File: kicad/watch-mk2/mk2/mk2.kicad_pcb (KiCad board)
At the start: 2 copper layers, 30 x 60 mm, 71 parts, among them IC1 113990582, IC2 M41T62LC6F, J1 FPC24-0.5mm, J2 USB_C_Receptacle_USB2.0, J3 Conn_01x02_Female, Q1 Si1308EDL, Q2 Si1308EDL, Q3 Si1308EDL, Q4 Si1308EDL, SW1 B5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

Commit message: add rev2mk2
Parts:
- removed C11, C12, C13, C14, C15, C16, C17, C18, C19: 1uF, Capacitor_SMD:C_0603_1608Metric_Pad1.05x0.95mm_HandSolder
- removed D3, D4, D5: MBR0530, Diode_SMD:D_SOD-123
- removed D6: CHRG_LED, LED_SMD:LED_0603_1608Metric_Pad1.05x0.95mm_HandSolder
- removed D7: FLASHLIGHT, Connector_PinHeader_2.54mm:PinHeader_1x02_P2.54mm_Vertical
- removed D8: BACKLIGHT, Connector_PinHeader_2.54mm:PinHeader_1x02_P2.54mm_Vertical
- removed Q1, Q2: Si1308EDL, Package_TO_SOT_SMD:SOT-323_SC-70
- removed R1, R2: 1k, Resistor_SMD:R_0603_1608Metric_Pad1.05x0.95mm_HandSolder
- removed R10: 470, Resistor_SMD:R_0603_1608Metric_Pad1.05x0.95mm_HandSolder
- removed R7: 10k, Resistor_SMD:R_0603_1608Metric_Pad1.05x0.95mm_HandSolder
- removed R8: 3, Resistor_SMD:R_0603_1608Metric_Pad1.05x0.95mm_HandSolder
- removed SW3: B2, libs:E-Switch-TL3330AF130QG-MFG
- removed SW5: B4, libs:E-Switch-TL3330AF130QG-MFG
- removed SW_BOOT1: SW_Push, Button_Switch_SMD:SW_SPST_CK_KXT3
- added J5: Conn_01x04_Female, libs:ffc-0.5mm-4, F.Cu at (31.2, 35.2)
- added JP1: FUEL_BYP, Resistor_SMD:R_0603_1608Metric, F.Cu at (34.6, 42.6)
- added P1: AXT610124, libs:PANASONIC_AXT610124, F.Cu at (31.5, 38.0)
- added U5: MAX17220ELT+, max17220:Maxim_Integrated-L622-1C-0-E-IPC_A, F.Cu at (18.0, 14.5)
- added U6: MAX17262REWL+T, max17262:Maxim-W91G1-3-0-A-IPC_A, F.Cu at (28.0, 45.0)
- BT1: footprint Connector_JST:JST_PH_B2B-PH-K_1x02_P2.00mm_Vertical -> Connector_JST:JST_SH_BM02B-SRSS-TB_1x02-1MP_P1.00mm_Vertical; moved to F.Cu
- C10: value 1uF -> 0.47uF; moved to F.Cu
- C20, D1, J2, R6, SW_RESET1: moved to F.Cu
- C6: value 4.7uF -> 10uF; moved to F.Cu
- C8: value 4.7uF -> 10uF
- C9: value 1uF -> 560pF; moved to F.Cu
- IC1: value 113990582 -> MDBT50Q
- J1: value FPC24-0.5mm -> Conn_01x10_Female; footprint Connector_FFC-FPC:Hirose_FH12-24S-0.5SH_1x24-1MP_P0.50mm_Horizontal -> Connector_FFC-FPC:Hirose_FH12-10S-0.5SH_1x10-1MP_P0.50mm_Horizontal
- L2: value 10uH -> 2.2uH
- R13, R15: value 1k -> 100k
- R5: value 10k -> 100k
- U1: footprint Package_SO:TSSOP-8_4.4x3mm_P0.65mm -> libs:SON50P300X200X60-9N
- moved C9 51.6 mm to (23.0, 15.4), turned to 90 degrees
- moved J1 48.0 mm to (29.5, 17.5), turned to 180 degrees
- moved J3 40.7 mm to (18.0, 17.5), turned to -90 degrees
- moved C8 39.3 mm to (23.0, 18.9), turned to 90 degrees
- moved L2 37.6 mm to (20.5, 14.6), turned to 90 degrees
- moved R15 35.1 mm to (14.4, 23.2), turned to 180 degrees
- moved C6 35.1 mm to (20.4, 17.5), turned to 180 degrees
- moved SW2 33.6 mm to (14.0, 16.8), turned to -90 degrees
- moved BT1 32.8 mm to (32.5, 47.0)
- moved Q4 31.2 mm to (14.2, 25.5), turned to 180 degrees
- moved J2 30.7 mm to (21.5, 44.8)
- moved R16 29.7 mm to (14.4, 21.8), turned to 180 degrees
- moved TP3 27.3 mm to (30.5, 24.8), turned to 180 degrees
- moved SW1 26.7 mm to (14.0, 31.2), turned to -90 degrees
- moved TP4 26.6 mm to (28.2, 27.0), turned to 180 degrees
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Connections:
- C10 pad 1: GND -> Net-(C10-Pad1)
- C10 pad 2: /EPVPP -> GND
- C20 pad 1: +BATT -> BATTPOW
- C6 pad 1: GND -> VIN
- C6 pad 2: VCC -> GND
- C8 pad 1: Net-(C8-Pad1) -> 5V
- C8 pad 2: Net-(C8-Pad2) -> GND
- C9 pad 1: /EPPREVGH -> LCD_DISP
- D1 pad 1: +BATT -> VUSB
- D1 pad 2: VUSB -> BATTPOW
- IC1 pad 10: BUTTON1 -> SPI_CLK
- IC1 pad 12: BUTTON5 -> SPI_MOSI
- IC1 pad 13: SQW -> BUZZER
- IC1 pad 14: RTCIRQ -> SPI_MISO
- IC1 pad 16: SCL -> FLASH_CS
- IC1 pad 19: SDA -> (no net)
- IC1 pad 20: FLASH_CS -> (no net)
- IC1 pad 22: FLASH_DO -> BUTTON1
- IC1 pad 24: FLASH_CLK -> BUTTON5
- IC1 pad 26: FLASH_DI -> BUTTON3
- IC1 pad 3: BOOTLOAD -> LCD_CS
- IC1 pad 36: FLASHLIGHT -> (no net)
- IC1 pad 41: (no net) -> RTCIRQ
- IC1 pad 42: (no net) -> SQW
- IC1 pad 43: EPSDIN -> (no net)
- IC1 pad 44: EPSCLK -> SDA
- IC1 pad 45: EPCS -> (no net)
- IC1 pad 46: EPDC -> SCL
- IC1 pad 47: EPRES -> (no net)
- IC1 pad 48: EPBUSY -> BUTTON4
- IC1 pad 49: (no net) -> FLASHLIGHT
- IC1 pad 50: (no net) -> BUTTON2
- IC1 pad 52: BUTTON3 -> CHGNG
- IC1 pad 54: BUTTON4 -> (no net)
- IC1 pad 6: BUZZER -> (no net)
- IC1 pad 8: BUTTON2 -> (no net)
- J1 pad 1: (no net) -> SPI_CLK
- J1 pad 10: EPRES -> GND
- J1 pad 2: /EPGDR -> SPI_MOSI
- J1 pad 3: /EPRESE -> LCD_CS
- J1 pad 4: /EPVGL -> SQW
- J1 pad 5: /EPVGH -> LCD_DISP
- J1 pad 6: (no net) -> 5V
- J1 pad 7: (no net) -> 5V
- J1 pad 8: GND -> 5V
- J1 pad 9: EPBUSY -> GND
- L2 pad 1: VCC -> VIN
- L2 pad 2: Net-(C8-Pad1) -> Net-(L2-Pad2)
- R5 pad 1: VCC -> CHGNG
- R5 pad 2: BOOTLOAD -> VCC
- TP1 pad 1: SWDIO -> GND
- TP4 pad 1: GND -> SWDIO
- U1 pad 2: FLASH_DO -> SPI_MISO
- U1 pad 5: FLASH_DI -> SPI_MOSI
- U1 pad 6: FLASH_CLK -> SPI_CLK
- U3 pad 1: Net-(R10-Pad1) -> CHGNG
- U3 pad 3: +BATT -> BATTPOW
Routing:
- net GND: track 66.2 -> 30.5 mm, vias 27 -> 33
- net EPSCLK: track 33.3 -> 0.00 mm, vias 2 -> 0
- net EPSDIN: track 31.5 -> 0.00 mm, vias 2 -> 0
- net EPCS: track 30.3 -> 0.00 mm, vias 2 -> 0
- net Net-(C8-Pad1): track 25.9 -> 0.00 mm, vias 2 -> 0
- net VCC: track 71.1 -> 46.0 mm, vias 14 -> 7
- net BATTPOW: track 0.00 -> 24.7 mm, vias 0 -> 4
- net VIN: track 25.5 -> 49.7 mm, vias 2 -> 6
- net EPRES: track 23.7 -> 0.00 mm, vias 2 -> 0
- net /EPPREVGH: track 23.6 -> 0.00 mm, vias 1 -> 0
- net EPDC: track 23.1 -> 0.00 mm, vias 2 -> 0
- net EPBUSY: track 22.7 -> 0.00 mm, vias 2 -> 0
- net SDA: track 9.68 -> 30.3 mm, vias 0 -> 3
- net SCL: track 7.17 -> 27.5 mm, vias 0 -> 3
- net CHGNG: track 0.00 -> 18.3 mm, vias 0 -> 4
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- added copper zone on In2.Cu, net GND
- added copper zone on In1.Cu, net VCC
- removed copper zone on B.Cu, net GND
- removed copper zone on F.Cu, net VCC
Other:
- board size 30 x 60 mm -> 23.5 x 37.5 mm
- copper layers 2 -> 4
- board text added: "+2.8v"
- board text added: "nrf52-watch mk2 - rev.2"
- board text removed: "+"
- board text removed: "+ -"
- board text removed: "+2.8V"
- board text removed: "-"
- board text removed: "Backlight"
- board text removed: "Flashlight"
- board text removed: "buzzer"
- board text removed: "nrf52-watch mk2 - rev.1"

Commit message: commit rev3
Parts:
- removed C5: 11mF, Capacitor_SMD:C_1210_3225Metric_Pad1.42x2.65mm_HandSolder
- removed C6, C8: 10uF, Capacitor_SMD:C_0603_1608Metric_Pad1.05x0.95mm_HandSolder
- removed D2: D_Schottky, Diode_SMD:D_0603_1608Metric_Pad1.05x0.95mm_HandSolder
- removed J5: Conn_01x04_Female, libs:ffc-0.5mm-4
- removed JP1: FUEL_BYP, Resistor_SMD:R_0603_1608Metric
- removed L2: 2.2uH, Inductor_SMD:L_0603_1608Metric_Pad1.05x0.95mm_HandSolder
- removed R5: 100k, Resistor_SMD:R_0603_1608Metric_Pad1.05x0.95mm_HandSolder
- removed U1: W25X20CLUXIG, libs:SON50P300X200X60-9N
- removed U5: MAX17220ELT+, max17220:Maxim_Integrated-L622-1C-0-E-IPC_A
- added J4: 503480-0400, libs:MOLEX_503480-0400, F.Cu at (32.5, 38.5)
- added U4: BMA400, libs:XDCR_BMA400, F.Cu at (21.5, 19.0)
- BT1: footprint Connector_JST:JST_SH_BM02B-SRSS-TB_1x02-1MP_P1.00mm_Vertical -> Connector_PinHeader_2.00mm:PinHeader_1x02_P2.00mm_Vertical
- J3: footprint Connector_PinHeader_1.00mm:PinHeader_1x02_P1.00mm_Vertical -> Connector_PinHeader_2.00mm:PinHeader_1x02_P2.00mm_Vertical
- moved C7 18.6 mm to (17.6, 33.2), turned to 0 degrees
- moved TP1 13.6 mm to (20.2, 13.8), turned to 90 degrees
- moved TP3 13.5 mm to (20.2, 16.0), turned to 90 degrees
- moved P1 11.7 mm to (20.0, 36.0), turned to 180 degrees
- moved IC2 6.36 mm to (17.5, 30.3), turned to 90 degrees
- moved J3 2.30 mm to (17.5, 15.2), turned to 0 degrees
- moved Q3 1.97 mm to (27.8, 33.9)
- moved SW_RESET1 1.97 mm to (25.0, 34.0)
- moved R6 1.32 mm to (22.0, 33.0), turned to 0 degrees
- moved BT1 1.12 mm to (31.5, 47.5), turned to 90 degrees
- moved U3 0.82 mm to (32.5, 42.5)
- moved R13 0.62 mm to (27.7, 37.0)
- moved R14 0.62 mm to (24.1, 37.0)
- moved C10 0.50 mm to (27.8, 48.1)
- moved SW1 0.50 mm to (13.5, 31.2)
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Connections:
- IC1 pad 14: SPI_MISO -> (no net)
- IC1 pad 16: FLASH_CS -> (no net)
- IC1 pad 21: BACKLIGHT -> (no net)
- IC1 pad 45: (no net) -> BACKLIGHT
- IC1 pad 7: (no net) -> ACCELINT1
- IC1 pad 9: (no net) -> ACCELINT2
- IC2 pad 5: Net-(C5-Pad1) -> VCC
- J1 pad 6: 5V -> VIN
- J1 pad 7: 5V -> VIN
- J1 pad 8: 5V -> VIN
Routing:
- net GND: track 30.5 -> 61.8 mm
- net 5V: track 17.6 -> 0.00 mm, vias 2 -> 0
- net SCL: track 27.5 -> 44.9 mm, vias 3 -> 8
- net SPI_MISO: track 10.6 -> 0.00 mm, vias 2 -> 0
- net SPI_CLK: track 16.6 -> 7.95 mm, vias 4 -> 0
- net ACCELINT1: track 0.00 -> 8.66 mm, vias 0 -> 2
- net FLASH_CS: track 8.53 -> 0.00 mm, vias 2 -> 0
- net ACCELINT2: track 0.00 -> 7.97 mm, vias 0 -> 2
- net SDA: track 30.3 -> 37.6 mm, vias 3 -> 8
- net Net-(C5-Pad1): track 7.06 -> 0.00 mm, vias 2 -> 0
- net +BATT: track 11.8 -> 5.80 mm
- net SPI_MOSI: track 13.2 -> 8.29 mm, vias 2 -> 0
- net BUTTON1: track 14.8 -> 10.5 mm
- net BATTPOW: track 24.7 -> 20.5 mm, vias 4 -> 2
- net VIN: track 49.7 -> 45.7 mm
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- added copper zone on B.Cu, net GND
- removed copper zone on In2.Cu, net GND
- removed copper zone on In1.Cu, net VCC
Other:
- copper layers 4 -> 2
- board text added: "+BATT"
- board text added: "buzzer"
- board text added: "nrf52-watch mk2 - rev.3 August 2020"
- board text removed: "nrf52-watch mk2 - rev.2"

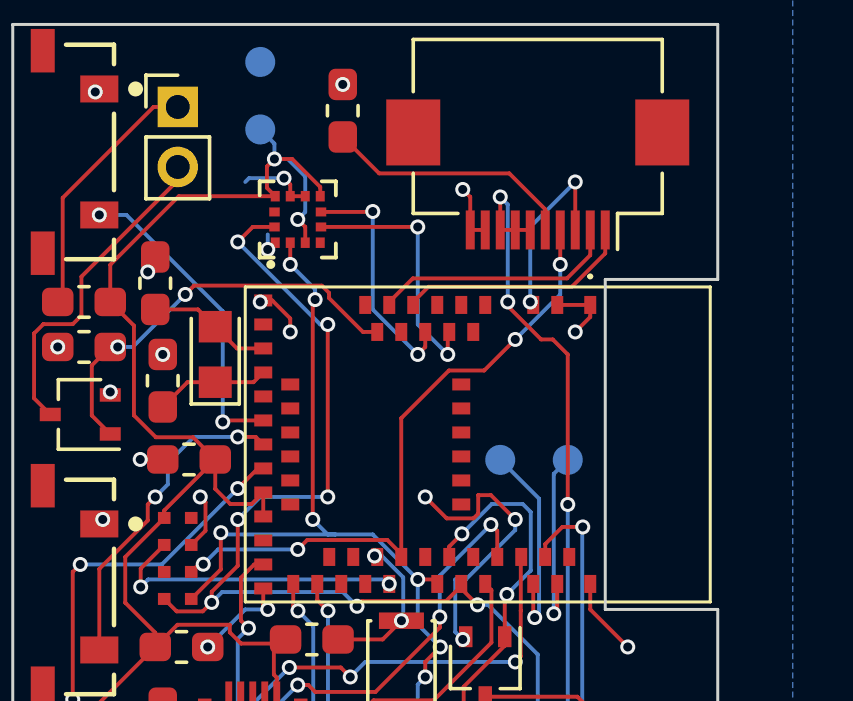
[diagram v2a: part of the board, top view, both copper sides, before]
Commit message: add rev2 of flex cable
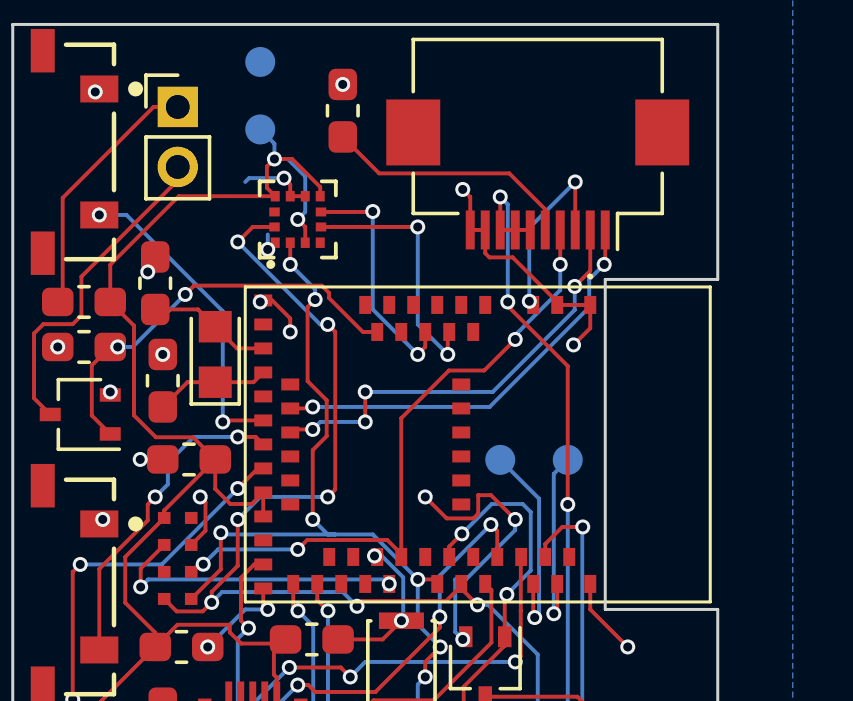
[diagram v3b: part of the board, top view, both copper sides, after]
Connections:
- IC1 pad 10: SPI_CLK -> (no net)
- IC1 pad 12: SPI_MOSI -> (no net)
- IC1 pad 21: (no net) -> SPI_CLK
- IC1 pad 23: (no net) -> SPI_MOSI
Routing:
- net SPI_MOSI: track 8.29 -> 14.6 mm, vias 0 -> 4
- net SPI_CLK: track 7.95 -> 14.2 mm, vias 0 -> 2
- net GND: track 61.8 -> 66.2 mm
- net SDA: track 37.6 -> 38.1 mm
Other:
- board text added: "nrf52-watch rev.3.1 August 2020"
- board text removed: "nrf52-watch mk2 - rev.3 August 2020"

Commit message: schematic checkpoint
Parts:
- added C5: 2.2uF, Capacitor_SMD:C_0603_1608Metric_Pad1.05x0.95mm_HandSolder, F.Cu at (20.0, 13.2)
- added C6: 2.2uF, Capacitor_SMD:C_0603_1608Metric_Pad1.05x0.95mm_HandSolder, F.Cu at (22.0, 15.4)
- added C8: 2.2uF, Capacitor_SMD:C_0603_1608Metric_Pad1.05x0.95mm_HandSolder, F.Cu at (17.9, 18.2)
- added J5: Conn_01x02_Female, Connector_PinHeader_2.00mm:PinHeader_1x02_P2.00mm_Vertical, F.Cu at (27.5, 47.8)
- added J6: Conn_01x02_Female, Connector_PinHeader_2.00mm:PinHeader_1x02_P2.00mm_Vertical, F.Cu at (20.5, 48.0)
- added TP5: TestPoint, TestPoint:TestPoint_Pad_D1.0mm, B.Cu at (31.8, 34.0)
- added TP6: TestPoint, TestPoint:TestPoint_Pad_D1.0mm, B.Cu at (28.2, 14.8)
- added U1: TPS60151DRV, Package_SON:WSON-6-1EP_2x2mm_P0.65mm_EP1x1.6mm_ThermalVias, F.Cu at (19.8, 15.5)
- R16: value 1k -> 10
- moved TP1 14.4 mm to (29.5, 24.8)
- moved C10 3.95 mm to (30.0, 44.9)
- moved TP3 2.69 mm to (22.8, 17.0)
- moved J3 1.03 mm to (17.2, 14.2)
- moved TP4 0.70 mm to (28.8, 27.5)
- moved BT1 0.56 mm to (32.0, 47.8)
- moved C9 0.50 mm to (23.5, 15.4)
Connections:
- IC1 pad 4: (no net) -> LCD_DISP
- J1 pad 6: VIN -> +5V
- J1 pad 7: VIN -> +5V
- J1 pad 8: VIN -> +5V
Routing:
- net VIN: track 45.5 -> 63.2 mm, vias 6 -> 7
- net +5V: track 0.00 -> 16.9 mm, vias 0 -> 1
- net GND: track 66.2 -> 81.6 mm, vias 33 -> 35
- net USB_DN: track 7.51 -> 13.4 mm
- net LCD_DISP: track 8.44 -> 12.6 mm, vias 0 -> 4
- net USB_DP: track 9.97 -> 14.1 mm
- net VCC: track 49.1 -> 45.9 mm, vias 2 -> 3
- net Net-(C6-Pad2): track 0.00 -> 2.69 mm
- net Net-(C6-Pad1): track 0.00 -> 2.58 mm
- net +BATT: track 5.80 -> 8.33 mm, vias 0 -> 2
- net Net-(C10-Pad1): track 4.11 -> 2.26 mm
- net SWDIO: track 6.99 -> 6.30 mm
- net BATTPOW: track 20.5 -> 19.9 mm
- net VUSB: track 36.3 -> 36.2 mm, vias 5 -> 7
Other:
- board text added: "+5V"
- board text added: "D+"
- board text added: "D-"
- board text added: "VIN"
- board text added: "VUSB"
- board text added: "nrf52-watch rev.4 September '20"
- board text removed: "nrf52-watch rev.3.1 August 2020"

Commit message: checkpoint
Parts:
- removed J5: Conn_01x02_Female, Connector_PinHeader_2.00mm:PinHeader_1x02_P2.00mm_Vertical
- removed P1: AXT610124, libs:PANASONIC_AXT610124
- removed R6: 10k, Resistor_SMD:R_0603_1608Metric_Pad1.05x0.95mm_HandSolder
- removed SW_RESET1: SW_Push, Button_Switch_SMD:SW_SPST_CK_KXT3
- added D2: D_Schottky_x2_KCom_AAK, Package_TO_SOT_SMD:TSOT-23, F.Cu at (22.6, 14.7)
- added JP1: Jumper_NO_Small, Jumper:SolderJumper-2_P1.3mm_Open_Pad1.0x1.5mm, B.Cu at (30.0, 16.8)
- added JP2: Jumper_NO_Small, Jumper:SolderJumper-2_P1.3mm_Open_Pad1.0x1.5mm, B.Cu at (25.4, 33.5)
- added JP3: Jumper_NC_Small, Jumper:SolderJumper-2_P1.3mm_Bridged_Pad1.0x1.5mm, B.Cu at (13.2, 39.2)
- added Q1: Si1308EDL, Package_TO_SOT_SMD:SOT-323_SC-70, F.Cu at (18.6, 37.8)
- added R1: shunt, Resistor_SMD:R_0603_1608Metric, B.Cu at (14.8, 39.4)
- added R2: 100k, Resistor_SMD:R_0603_1608Metric_Pad1.05x0.95mm_HandSolder, F.Cu at (20.4, 34.8)
- added U5: TPD2S017, Package_TO_SOT_SMD:SOT-23-6, F.Cu at (23.6, 39.6)
- J2: value USB_C_Receptacle_USB2.0 -> 2305018-2; footprint Connector_USB:USB_C_Receptacle_Palconn_UTC16-G -> te-waterproof-usb-2305018-2:TE_2305018-2
- J6: footprint Connector_PinHeader_2.00mm:PinHeader_1x02_P2.00mm_Vertical -> Connector_PinSocket_2.00mm:PinSocket_1x02_P2.00mm_Vertical
- R14: value 1k -> 100
- moved J3 14.8 mm to (18.4, 29.0)
- moved J6 12.3 mm to (18.6, 35.8), turned to 180 degrees
- moved IC2 11.6 mm to (22.9, 20.1), turned to 180 degrees
- moved R14 6.03 mm to (29.7, 39.2), turned to -90 degrees
- moved R11 5.65 mm to (27.2, 42.7)
- moved C6 4.78 mm to (17.4, 14.1), turned to 180 degrees
- moved C8 4.65 mm to (20.2, 14.2), turned to 90 degrees
- moved R13 3.66 mm to (28.8, 33.5), turned to 180 degrees
- moved R12 3.54 mm to (28.6, 42.7)
- moved C5 3.53 mm to (20.3, 16.8), turned to 0 degrees
- moved R9 3.50 mm to (30.0, 42.7)
- moved R3 3.10 mm to (26.9, 38.5), turned to 180 degrees
- moved TP4 3.02 mm to (26.0, 26.2)
- moved C9 2.91 mm to (23.5, 18.3), turned to 180 degrees
- moved C10 2.88 mm to (30.0, 47.8)
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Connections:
- D1 pad 3: VIN -> Net-(D1-Pad3)
- IC1 pad 16: (no net) -> 5VREG_EN
- IC1 pad 48: BUTTON4 -> (no net)
- IC1 pad 50: BUTTON2 -> (no net)
- J1 pad 6: +5V -> DISP_POWER
- J1 pad 7: +5V -> DISP_POWER
- J1 pad 8: +5V -> DISP_POWER
- J2 pad A5: Net-(J2-PadA5) -> Net-(R12-Pad2)
- J2 pad A6: USB_DP -> USB_DP_EXT
- J2 pad A7: USB_DN -> USB_DN_EXT
- J2 pad B5: Net-(J2-PadB5) -> Net-(R11-Pad1)
- J2 pad B6: USB_DP -> USB_DP_EXT
- J2 pad B7: USB_DN -> USB_DN_EXT
- J6 pad 1: USB_DN -> VIN
- J6 pad 2: USB_DP -> Net-(J6-Pad2)
- R11 pad 1: Net-(J2-PadA5) -> Net-(R11-Pad1)
- R12 pad 1: Net-(J2-PadB5) -> GND
- R12 pad 2: GND -> Net-(R12-Pad2)
- U1 pad 6: VIN -> 5VREG_EN
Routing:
- net BUTTON2: track 15.2 -> 0.00 mm, vias 4 -> 0
- net GND: track 81.6 -> 96.4 mm, vias 35 -> 31
- net BUTTON4: track 13.1 -> 0.00 mm
- net DISP_POWER: track 0.00 -> 12.4 mm, vias 0 -> 1
- net USB_DP: track 14.1 -> 1.83 mm, vias 3 -> 0
- net USB_DN: track 13.4 -> 1.43 mm
- net 5VREG_EN: track 0.00 -> 11.7 mm
- net Net-(R12-Pad2): track 0.00 -> 9.97 mm, vias 0 -> 2
- net FLASHLIGHT: track 14.3 -> 22.5 mm
- net USB_DN_EXT: track 0.00 -> 8.07 mm, vias 0 -> 4
- net ACCELINT2: track 7.79 -> 15.5 mm, vias 2 -> 4
- net Net-(D1-Pad3): track 0.00 -> 7.31 mm, vias 0 -> 1
- net BACKLIGHT: track 14.2 -> 7.20 mm
- net Net-(R11-Pad1): track 0.00 -> 6.48 mm
- net SDA: track 38.1 -> 44.6 mm, vias 8 -> 6
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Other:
- outline, holes or cut-outs redrawn
- board text added: "+"
- board text added: "-"
- board text added: "nrf52-watch rev. 6.1 March '21"
- board text added: "rst"
- board text removed: "D+"
- board text removed: "D-"
- board text removed: "VUSB"
- board text removed: "nrf52-watch rev.4 September '20"

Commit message: checkpoint
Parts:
- JP2: moved to F.Cu
- moved D1 1.17 mm to (19.5, 40.6)
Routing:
- net GND: track 96.4 -> 99.5 mm
- net Net-(D1-Pad3): track 7.31 -> 5.00 mm
- net USB_DP_EXT: track 5.59 -> 7.62 mm, vias 0 -> 2
- net Net-(IC1-Pad35): track 12.5 -> 13.6 mm
- net BATTPOW: track 24.9 -> 25.7 mm
- net RST: track 5.65 -> 5.76 mm, vias 1 -> 2
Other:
- board text added: "nrf52-watch rev. 7 Dec '21"
- board text removed: "nrf52-watch rev. 6.1 March '21"
